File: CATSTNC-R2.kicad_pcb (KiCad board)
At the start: 2 copper layers, 79 x 59.5 mm, 74 parts, among them J1 BNC, J4 USB_C_Receptacle_USB2.0, J5 DC IN, J6 GPIO-1, J7 GPIO-2, SW1 RESET, SW2 BOOT, U1 TPS62933, U2 W25Q128JVS, U3 RP2040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

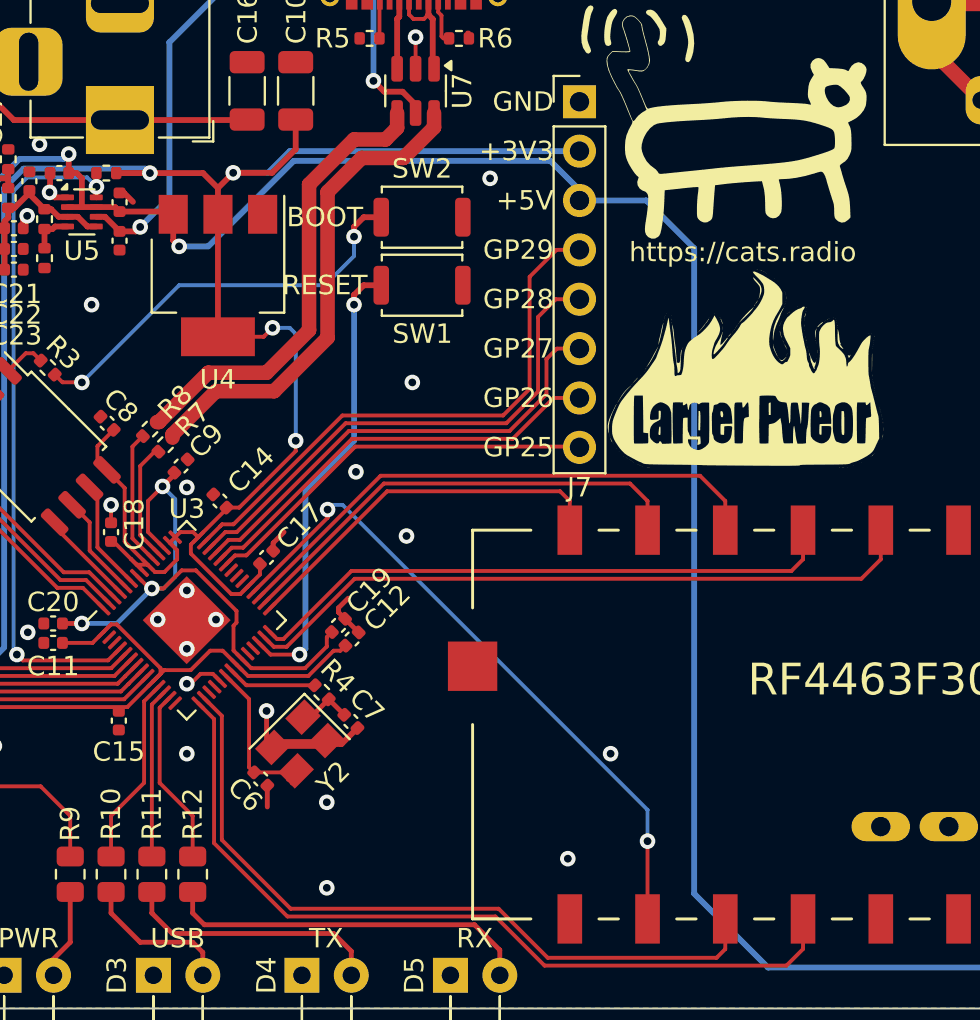
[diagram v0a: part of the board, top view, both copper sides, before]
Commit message: Add SWD header, VCC voltmeter, replace GP29 with VIN
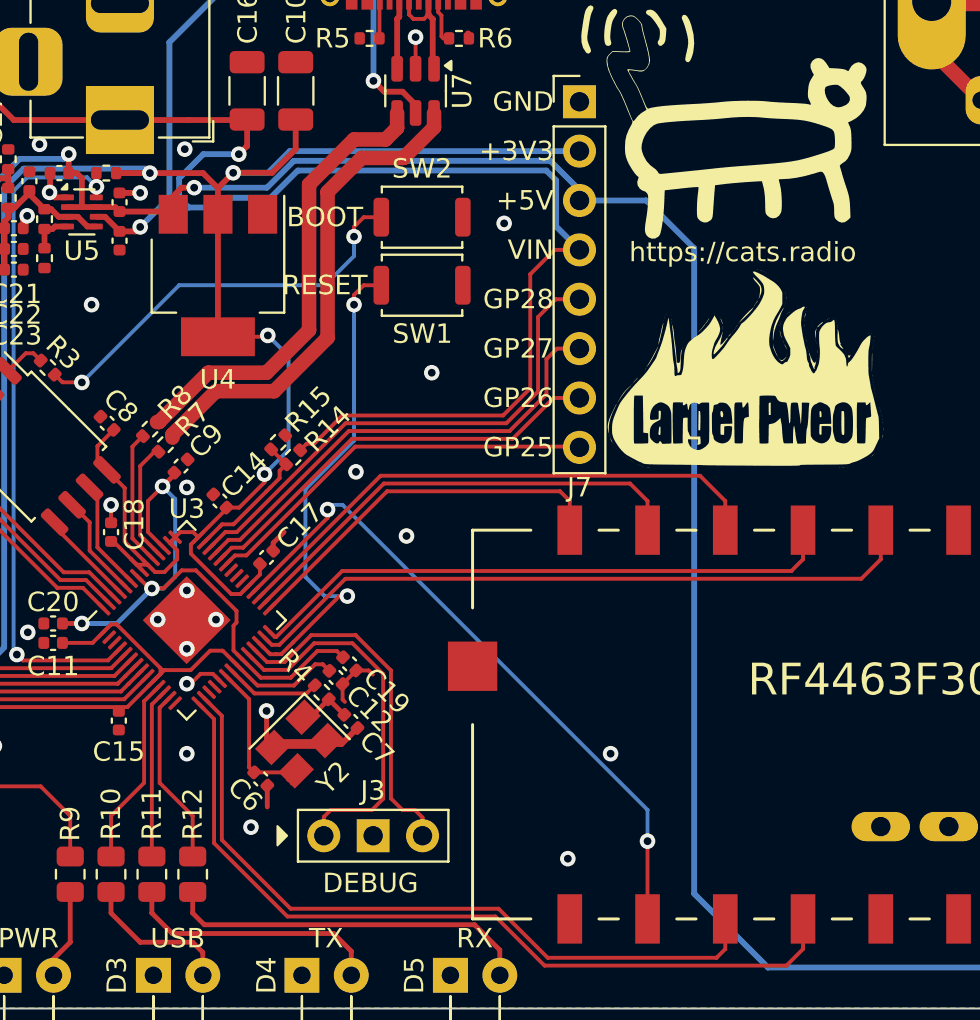
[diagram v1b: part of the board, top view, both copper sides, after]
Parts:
- added J3: DEBUG, Connector_PinHeader_2.54mm:PinHeader_1x03_P2.54mm_Vertical, F.Cu at (131.9, 113.3)
- added R14: 54.9K 1%, Resistor_SMD:R_0402_1005Metric, F.Cu at (130.4, 93.8)
- added R15: 10.0K 1%, Resistor_SMD:R_0402_1005Metric, F.Cu at (129.6, 93.1)
- moved C12 2.14 mm to (132.6, 105.2), turned to -45 degrees
- moved C19 2.06 mm to (133.3, 104.5), turned to -45 degrees
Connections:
- J7 pad 4: GP29 -> VCC
- U3 pad 24: unconnected-(U3-SWCLK-Pad24) -> SWCLK
- U3 pad 25: unconnected-(U3-SWD-Pad25) -> SWD
- U3 pad 41: GP29 -> VCC_VOLTS
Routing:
- net VCC: track 21.7 -> 75.0 mm, vias 0 -> 1
- net GP29: track 29.0 -> 0.00 mm
- net SWCLK: track 0.00 -> 19.5 mm
- net SWD: track 0.00 -> 18.3 mm
- net VCC_VOLTS: track 0.00 -> 7.22 mm
- net +3V3: track 167.5 -> 165.3 mm
- net Net-(U3-RUN): track 23.6 -> 25.8 mm
- net +5V: track 137.7 -> 136.1 mm
- net GND: track 24.9 -> 26.0 mm, vias 25 -> 26
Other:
- board text added: "DEBUG"
- board text added: "VIN"
- board text removed: "GP29"

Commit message: Did some stuff idk
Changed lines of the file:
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@@
 		(tags "capacitor")
 		(property "Reference" "C1"
-			(at -0.739999 1.308012 90)
+			(at -0.005232 1.371086 90)
 			(layer "F.SilkS")
 			(effects

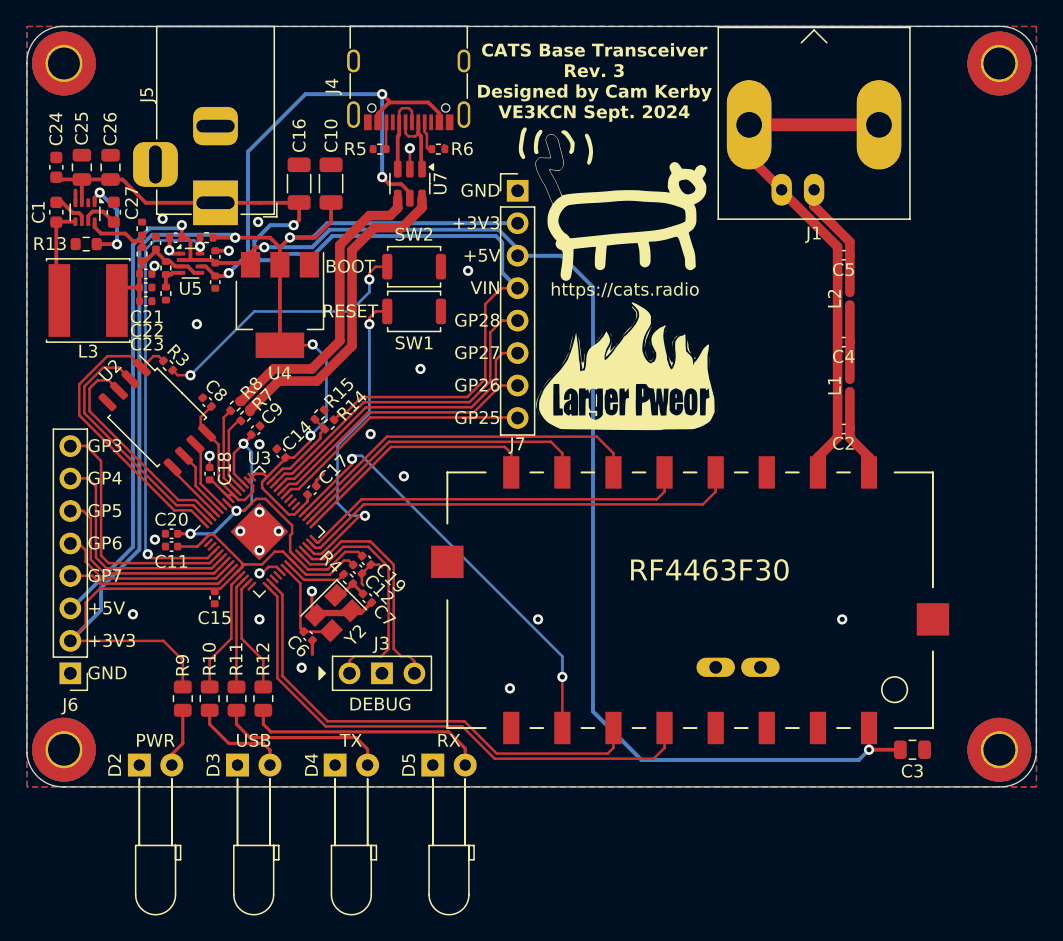
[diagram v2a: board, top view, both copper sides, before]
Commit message: Made some small optimizations: see full commit message.
* Changed PCB text font to Liberation Sans
* Re-added semiconductor part values to front silkscreen
* Moved GPIO header closer to edge of board, per general practice
* Moved some existing silkscreen messages
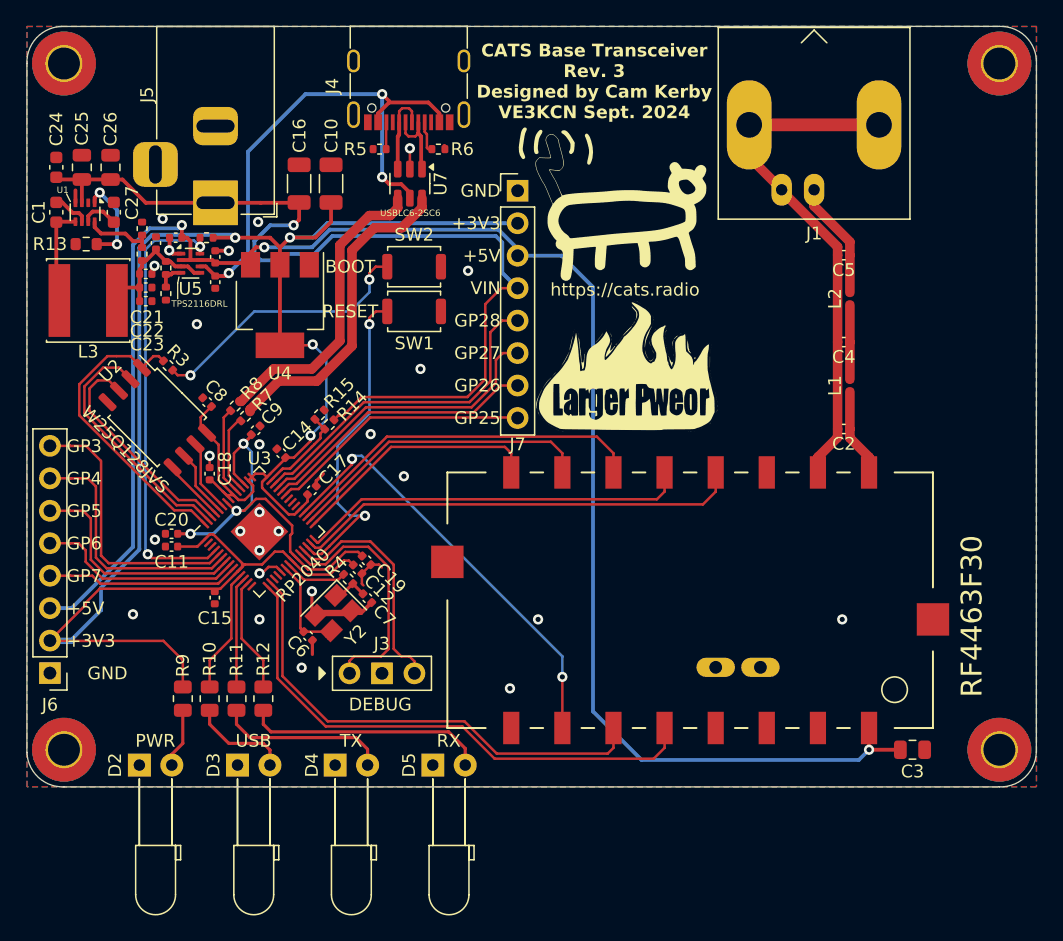
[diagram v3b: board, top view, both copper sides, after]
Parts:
- moved J6 1.60 mm to (108.5, 113.3)
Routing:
- net +3V3: track 165.3 -> 170.7 mm
- net GP5: track 16.5 -> 18.1 mm
- net GP3: track 20.1 -> 21.7 mm
- net GP6: track 14.6 -> 16.2 mm
- net GP4: track 18.5 -> 20.1 mm
- net GP7: track 14.1 -> 15.1 mm
- net +5V: track 136.1 -> 136.9 mm
